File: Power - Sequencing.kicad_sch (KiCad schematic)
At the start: 0 parts

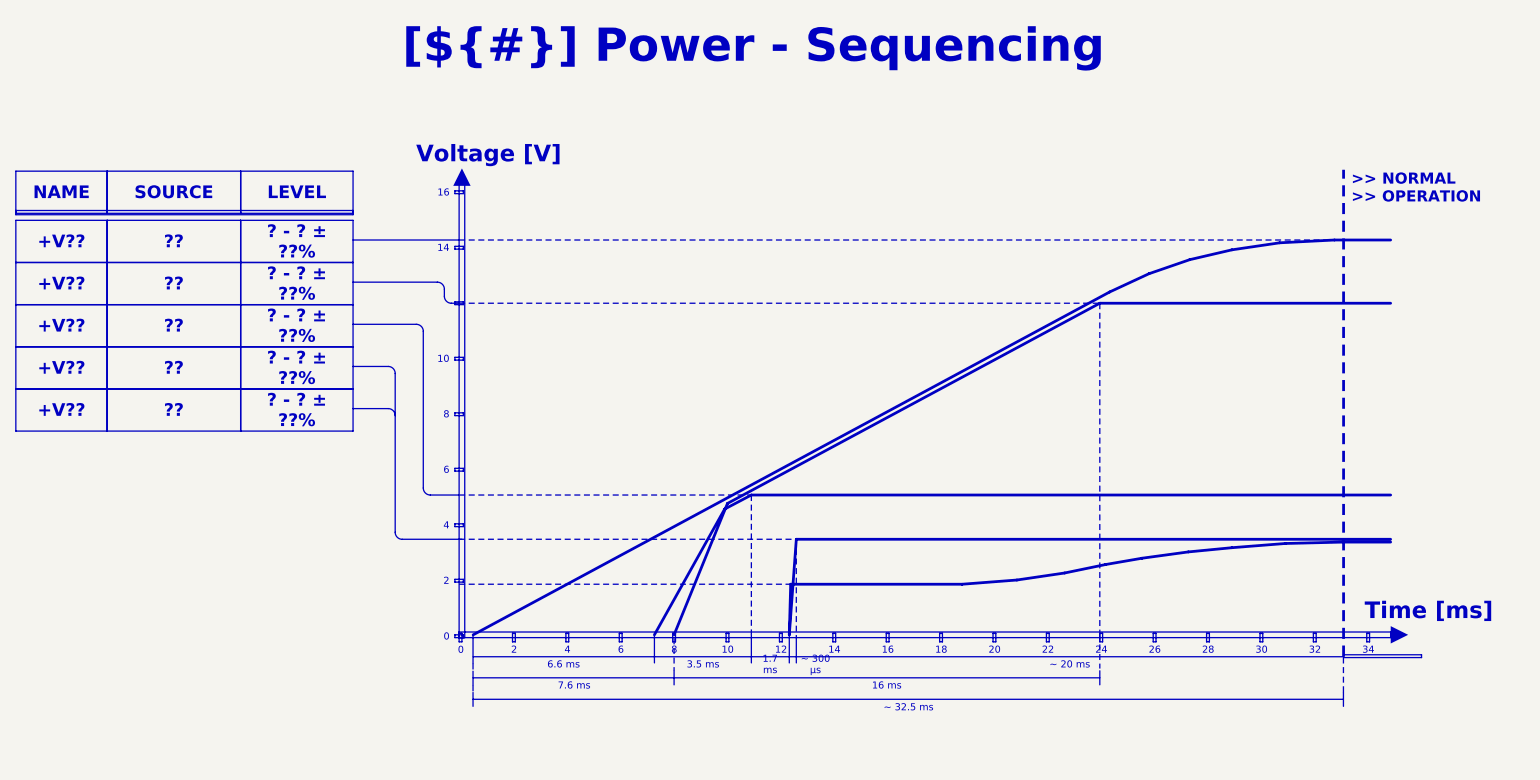
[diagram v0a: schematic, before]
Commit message: documentation update / release 2.1.1 prep
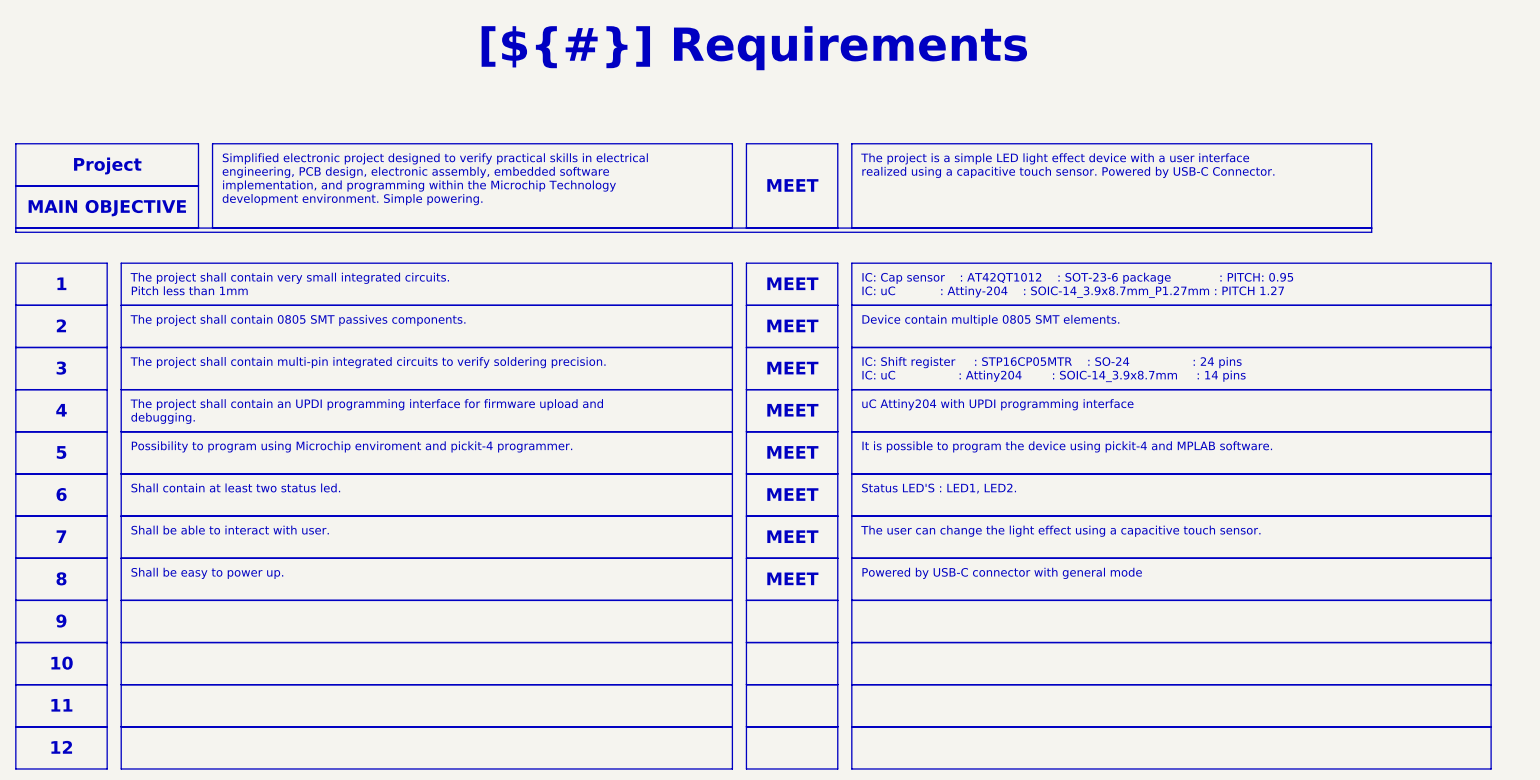
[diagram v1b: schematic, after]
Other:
- note removed: ">> NORMAL >> OPERATION"
- note removed: "Time [ms]"
- note removed: "Voltage [V]"
- title: Power - Sequencing -> Requirements
